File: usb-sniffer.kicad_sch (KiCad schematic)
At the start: 3 parts, among them J1 USB_C_Receptacle_USB2.0_16P

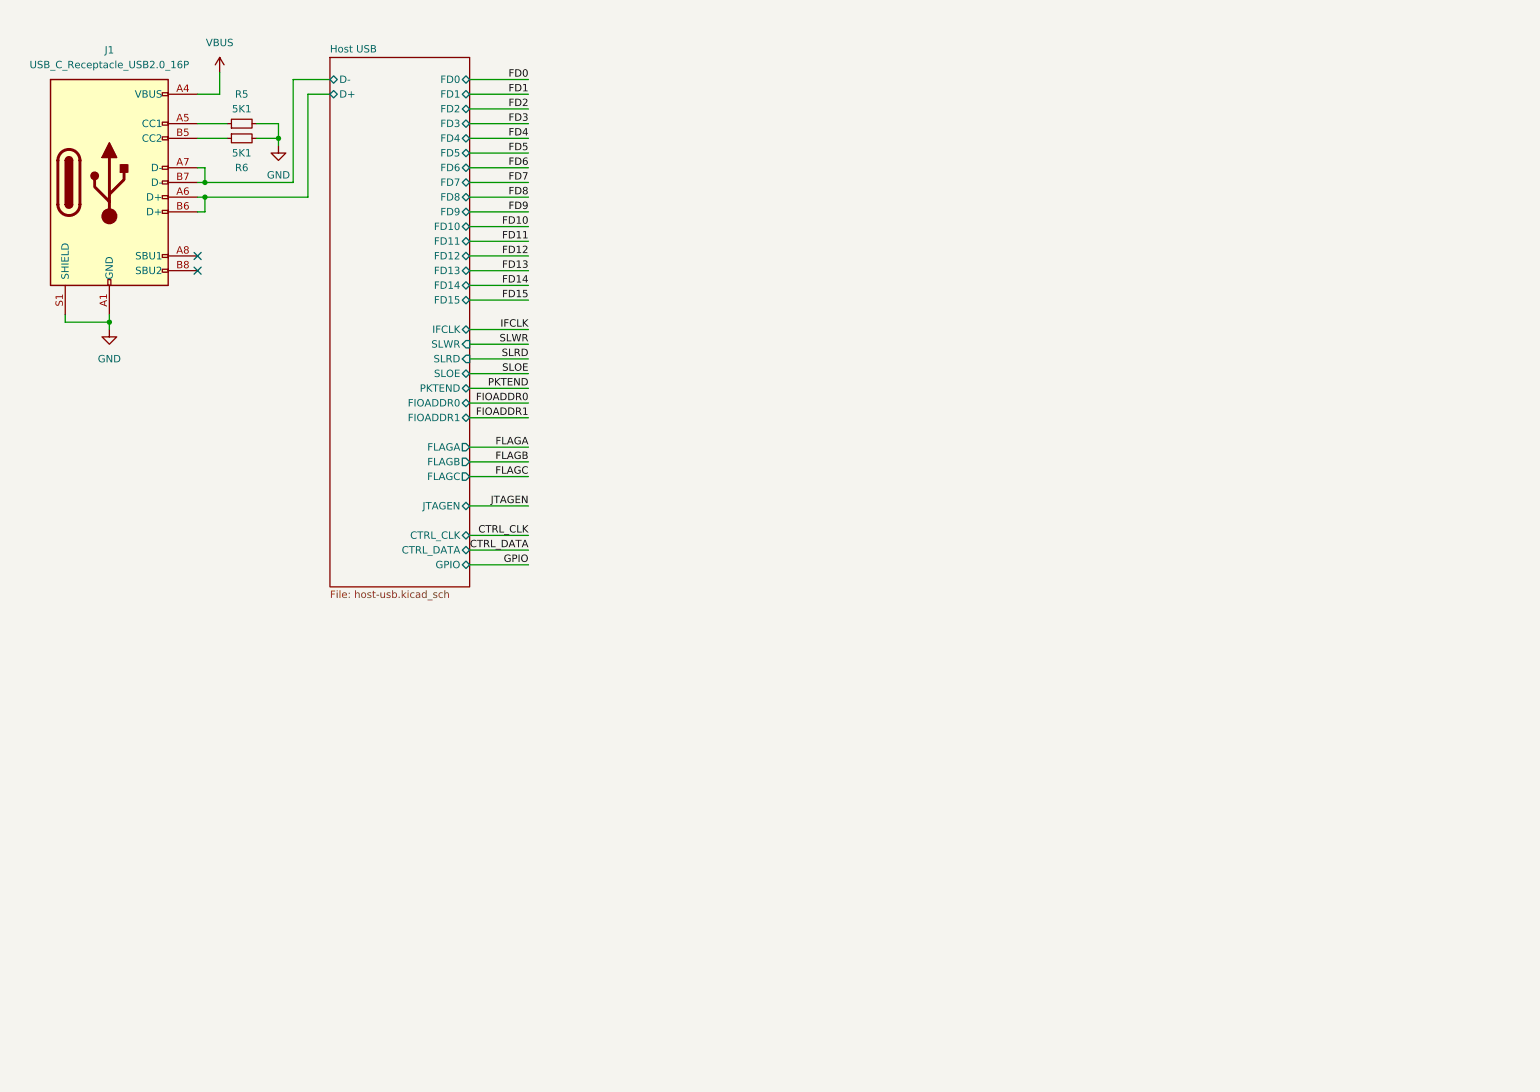
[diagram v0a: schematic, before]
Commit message: Add USB3343
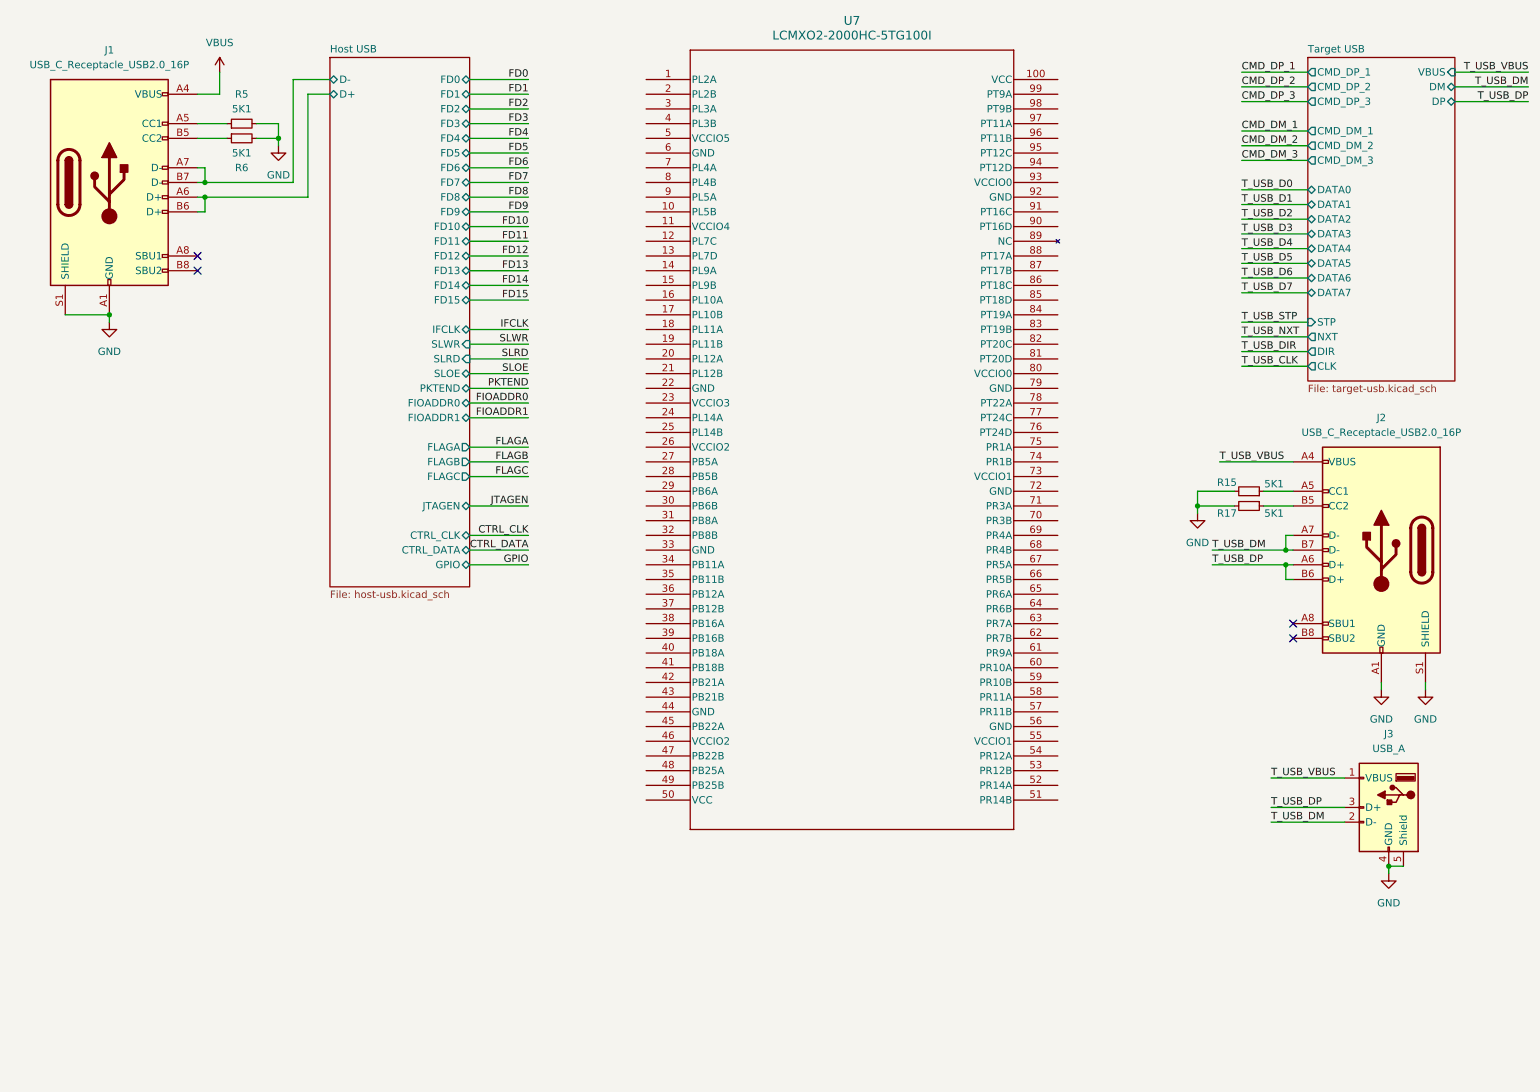
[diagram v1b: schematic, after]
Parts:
- added J2: USB_C_Receptacle_USB2.0_16P, Connector_USB:USB_C_Receptacle_G-Switch_GT-USB-7010ASV, symbol Connector:USB_C_Receptacle_USB2.0_16P
- added J3: USB_A, Connector_USB:USB_A_Molex_67643_Horizontal, symbol Connector:USB_A
- added R15, R17: 5K1, Resistor_SMD:R_0402_1005Metric, symbol Device:R_Small
- added U7: LCMXO2-2000HC-5TG100I, TQFP100_LAT, symbol 2024-03-04_09-59-19:LCMXO2-2000HC-5TG100I
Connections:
- net GND: now also J2.A1 (GND), J2.A12 (GND), J2.B1 (GND), J2.B12 (GND), J2.S1 (SHIELD), J3.4 (GND), J3.5 (Shield), R15.2, R17.2
- new net: J2.A5 (CC1), R15.1
- new net: J2.B5 (CC2), R17.1
- new net T_USB_DM: J2.A7 (D-), J2.B7 (D-), J3.2 (D-)
- new net T_USB_DP: J2.A6 (D+), J2.B6 (D+), J3.3 (D+)
- new net T_USB_VBUS: J2.A4 (VBUS), J2.A9 (VBUS), J2.B4 (VBUS), J2.B9 (VBUS), J3.1 (VBUS)
- no-connect marks 2 -> 4
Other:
- added sheet Target USB (target-usb.kicad_sch)

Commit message: layout uncompleted
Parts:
- added C24, C25, C26, C27, C28, C29, C30, C31: 100nF, Capacitor_SMD:C_0402_1005Metric, symbol Device:C_Small
- added D1, D3, D4, D5: LED, LED_SMD:LED_0603_1608Metric, symbol Device:LED
- added R18: 10K, Resistor_SMD:R_0402_1005Metric, symbol Device:R_Small
- added R19, R20, R21, R22: 2K2, Resistor_SMD:R_0402_1005Metric, symbol Device:R_Small
- added TP1, TP2, TP3, TP4, TP5, TP6, TP7, TP8: Test, TestPoint:TestPoint_Pad_D1.0mm, symbol Connector:TestPoint
- U7: footprint TQFP100_LAT -> Package_QFP:LQFP-100_14x14mm_P0.5mm
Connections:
- net CMD_DM_1: now also U7.96 (PT11B)
- net CMD_DM_2: now also U7.97 (PT11A)
- net CMD_DM_3: now also U7.98 (PT9B)
- net CMD_DP_1: now also U7.3 (PL3A)
- net CMD_DP_2: now also U7.2 (PL2B)
- net CMD_DP_3: now also U7.1 (PL2A)
- net CTRL_CLK: now also U7.71 (PR3A)
- net CTRL_DATA: now also U7.68 (PR4B)
- net FD0: now also U7.90 (PT16D)
- net FD1: now also U7.91 (PT16C)
- net FD10: now also U7.53 (PR12B)
- net FD11: now also U7.52 (PR14A)
- net FD12: now also U7.51 (PR14B)
- net FD13: now also U7.43 (PB21B)
- net FD14: now also U7.45 (PB22A)
- net FD15: now also U7.47 (PB22B)
- net FD2: now also U7.94 (PT12D)
- net FD3: now also U7.95 (PT12C)
- net FD4: now also U7.87 (PT17B)
- net FD5: now also U7.86 (PT18C)
- net FD6: now also U7.85 (PT18D)
- net FD7: now also U7.84 (PT19A)
- net FD8: now also U7.57 (PR11B)
- net FD9: now also U7.54 (PR12A)
- net FIOADDR0: now also U7.67 (PR5A)
- net FIOADDR1: now also U7.65 (PR6A)
- net FLAGA: now also U7.78 (PT22A)
- net FLAGB: now also U7.75 (PR1A)
- net FLAGC: now also U7.74 (PR1B)
- net GND: now also U7.22 (GND), U7.33 (GND), U7.44 (GND), U7.56 (GND), U7.6 (GND), U7.72 (GND), U7.79 (GND), U7.92 (GND), C24.2, C25.2, C26.2, C27.2, C28.2, C29.2, C30.2, C31.2, R19.2, R20.2, R21.2, R22.2, TP8.1
- net GPIO: now also U7.63 (PR7A)
- net IFCLK: now also U7.88 (PT17A)
- net JTAGEN: now also U7.70 (PR3B), U7.82 (PT20C), R18.1
- net PKTEND: now also U7.64 (PR6B)
- net SLOE: now also U7.69 (PR4A)
- net SLRD: now also U7.48 (PB25A)
- net SLWR: now also U7.49 (PB25B)
- net T_USB_CLK: now also U7.20 (PL12A)
- net T_USB_D0: now also U7.18 (PL11A)
- net T_USB_D1: now also U7.17 (PL10B)
- net T_USB_D2: now also U7.16 (PL10A)
- net T_USB_D3: now also U7.15 (PL9B)
- net T_USB_D4: now also U7.13 (PL7D)
- net T_USB_D5: now also U7.10 (PL5B)
- net T_USB_D6: now also U7.9 (PL5A)
- net T_USB_D7: now also U7.8 (PL4B)
- net T_USB_DIR: now also U7.21 (PL12B)
- net T_USB_NXT: now also U7.19 (PL11B)
- net T_USB_STP: now also U7.24 (PL14A)
- net +3V3: now reaches U7.100 (VCC)
- net +3V3: now also U7.11 (VCCIO4), U7.23 (VCCIO3), U7.26 (VCCIO2), U7.46 (VCCIO2), U7.5 (VCCIO5), U7.50 (VCC), U7.55 (VCCIO1), U7.73 (VCCIO1), U7.80 (VCCIO0), U7.93 (VCCIO0), C24.1, C25.1, C26.1, C27.1, C28.1, C29.1, C30.1, C31.1, R18.2
- net DBG_3: now reaches U7.29 (PB6A)
- net DBG_3: now also D5.2 (A)
- net DBG_2: now reaches U7.30 (PB6B)
- net DBG_2: now also D4.2 (A)
- net DBG_1: now reaches U7.31 (PB8A)
- net DBG_1: now also D3.2 (A)
- net DBG_0: now reaches U7.32 (PB8B)
- net DBG_0: now also D1.2 (A)
- net SPARE_0: now reaches U7.34 (PB11A)
- net SPARE_0: now also TP1.1
- net SPARE_1: now reaches U7.35 (PB11B)
- net SPARE_1: now also TP2.1
- net SPARE_2: now reaches U7.36 (PB12A)
- net SPARE_2: now also TP3.1
- net SPARE_3: now reaches U7.37 (PB12B)
- net SPARE_3: now also TP4.1
- net SPARE_4: now reaches U7.38 (PB16A)
- net SPARE_4: now also TP5.1
- net SPARE_5: now reaches U7.39 (PB16B)
- net SPARE_5: now also TP6.1
- net SPARE_6: now reaches U7.40 (PB18A)
- net SPARE_6: now also TP7.1
- net T_USB_DM renamed T_USB_DN
- new net: D5.1 (K), R22.1
- new net: D4.1 (K), R21.1
- new net: D3.1 (K), R20.1
- new net: D1.1 (K), R19.1
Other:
- sheet Target USB ports: added DN; removed DM
- moved on the sheet: U7

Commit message: add side ground
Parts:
- added D6: BAT54S, Package_TO_SOT_SMD:SOT-23, symbol Diode:BAT54S
- added J4: Conn_01x02, Connector_PinHeader_2.54mm:PinHeader_1x02_P2.54mm_Vertical, symbol Connector_Generic:Conn_01x02
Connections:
- net +3V3: now also D6.2 (K)
- net GND: now also D6.1 (A), J4.2 (Pin_2)
- net IO_IN: now reaches U7.41 (PB18B)
- net IO_IN: now also D6.3 (COM), J4.1 (Pin_1)
